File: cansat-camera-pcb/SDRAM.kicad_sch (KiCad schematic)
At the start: 10 parts, among them IC1 W9825G6JB-6I

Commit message: CODEGEN + finishing SDRAM routing
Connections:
- net A0: now also IC1.H7 (A0); no longer IC1.H9 (A10)
- net A1: now also IC1.H8 (A1); no longer IC1.J8 (A2)
- net A10: now also IC1.H9 (A10); no longer IC1.G2 (A11)
- net A11: now also IC1.G2 (A11); no longer IC1.H8 (A1)
- net A12: now also IC1.G1 (A12); no longer IC1.G3 (A9)
- net A2: now also IC1.J8 (A2); no longer IC1.J7 (A3)
- net A3: now also IC1.J7 (A3); no longer IC1.H7 (A0)
- net A7: now also IC1.H2 (A7); no longer IC1.H1 (A8)
- net A8: now also IC1.H1 (A8); no longer IC1.H2 (A7)
- net A9: now also IC1.G3 (A9); no longer IC1.G1 (A12)
- net DQ0: now also IC1.A8 (DQ0); no longer IC1.B8 (DQ2)
- net DQ1: now also IC1.B9 (DQ1); no longer IC1.A8 (DQ0)
- net DQ10: now also IC1.D1 (DQ10); no longer IC1.D2 (DQ9)
- net DQ11: now also IC1.C2 (DQ11); no longer IC1.C1 (DQ12)
- net DQ12: now also IC1.C1 (DQ12); no longer IC1.C2 (DQ11)
- net DQ13: now also IC1.B2 (DQ13); no longer IC1.B1 (DQ14)
- net DQ14: now also IC1.B1 (DQ14); no longer IC1.B2 (DQ13)
- net DQ2: now also IC1.B8 (DQ2); no longer IC1.B9 (DQ1)
- net DQ4: now also IC1.C8 (DQ4); no longer IC1.E9 (DQ7)
- net DQ7: now also IC1.E9 (DQ7); no longer IC1.C8 (DQ4)
- net DQ9: now also IC1.D2 (DQ9); no longer IC1.D1 (DQ10)

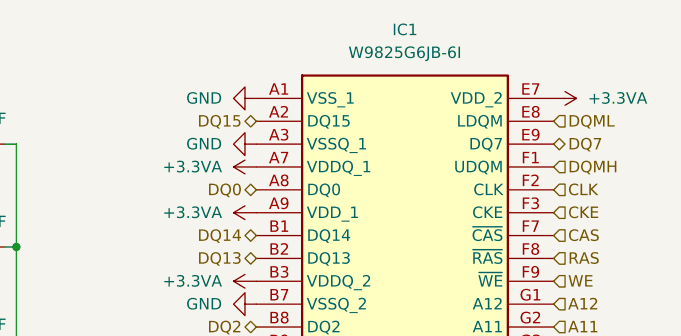
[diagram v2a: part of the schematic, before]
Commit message: OV5640 routing start
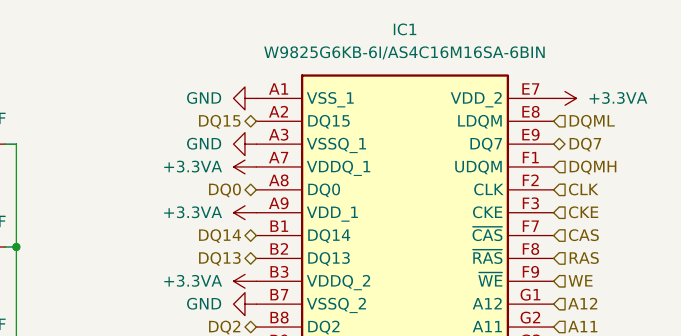
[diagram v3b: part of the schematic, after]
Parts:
- IC1: value W9825G6JB-6I -> W9825G6KB-6I/AS4C16M16SA-6BIN; Manufacturer_Part_Number W9825G6JB-6I -> W9825G6KB-6I
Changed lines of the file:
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@@
 			)
 		)
-		(property "Value" "W9825G6JB-6I"
+		(property "Value" "W9825G6KB-6I/AS4C16M16SA-6BIN"
 			(at 93.98 22.86 0)
 			(effects
@@
 			)
 		)
-		(property "Manufacturer_Part_Number" "W9825G6JB-6I"
+		(property "Manufacturer_Part_Number" "W9825G6KB-6I"
 			(at 106.68 822.86 0)
 			(effects

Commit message: Production v1.3+1.2
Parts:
- added R25, R26, R27, R28, R29, R30, R31, R32, R33, R34, R35, R36, R37, R38, R39, R40, R41: 22, Resistor_SMD:R_0201_0603Metric, symbol Device:R_Small
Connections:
- net CLK: now also R41.2; no longer IC1.F2 (CLK)
- net DQ0: now also R38.1; no longer IC1.A8 (DQ0)
- net DQ1: now also R34.1; no longer IC1.B9 (DQ1)
- net DQ10: now also R29.1; no longer IC1.D1 (DQ10)
- net DQ11: now also R32.1; no longer IC1.C2 (DQ11)
- net DQ12: now also R33.1; no longer IC1.C1 (DQ12)
- net DQ13: now also R36.1; no longer IC1.B2 (DQ13)
- net DQ14: now also R37.1; no longer IC1.B1 (DQ14)
- net DQ15: now also R39.1; no longer IC1.A2 (DQ15)
- net DQ2: now also R35.1; no longer IC1.B8 (DQ2)
- net DQ3: now also R30.1; no longer IC1.C9 (DQ3)
- net DQ4: now also R31.1; no longer IC1.C8 (DQ4)
- net DQ5: now also R26.1; no longer IC1.D9 (DQ5)
- net DQ6: now also R27.1; no longer IC1.D8 (DQ6)
- net DQ7: now also R40.2; no longer IC1.E9 (DQ7)
- net DQ8: now also R25.1; no longer IC1.E1 (DQ8)
- net DQ9: now also R28.1; no longer IC1.D2 (DQ9)
- new net: IC1.D8 (DQ6), R27.2
- new net: IC1.A2 (DQ15), R39.2
- new net: IC1.A8 (DQ0), R38.2
- new net: IC1.B1 (DQ14), R37.2
- new net: IC1.C1 (DQ12), R33.2
- new net: IC1.B9 (DQ1), R34.2
- new net: IC1.E1 (DQ8), R25.2
- new net: IC1.E9 (DQ7), R40.1
- new net: IC1.F2 (CLK), R41.1
- new net: IC1.B2 (DQ13), R36.2
- new net: IC1.B8 (DQ2), R35.2
- new net: IC1.C2 (DQ11), R32.2
- new net: IC1.C8 (DQ4), R31.2
- new net: IC1.C9 (DQ3), R30.2
- new net: IC1.D1 (DQ10), R29.2
- new net: IC1.D2 (DQ9), R28.2
- new net: IC1.D9 (DQ5), R26.2
